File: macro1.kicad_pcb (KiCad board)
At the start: 2 copper layers, 65.9 x 38.1 mm, 24 parts, among them SW1 SW_Push, U1 ATmega32U4-A, Y1 Crystal

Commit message: First Route: NoKeys
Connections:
- U1 pad 27: unconnected-(U1-Pad27) -> ROW0
- U1 pad 28: unconnected-(U1-Pad28) -> COL1
- U1 pad 29: unconnected-(U1-Pad29) -> COL0
- U1 pad 30: unconnected-(U1-Pad30) -> ROW1
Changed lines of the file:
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@@
   (net 31 "unconnected-(U1-Pad25)")
   (net 32 "unconnected-(U1-Pad26)")
-  (net 33 "unconnected-(U1-Pad27)")
-  (net 34 "unconnected-(U1-Pad28)")
-  (net 35 "unconnected-(U1-Pad29)")
-  (net 36 "unconnected-(U1-Pad30)")
-  (net 37 "unconnected-(U1-Pad31)")
-  (net 38 "unconnected-(U1-Pad32)")
-  (net 39 "unconnected-(U1-Pad36)")
-  (net 40 "unconnected-(U1-Pad37)")
-  (net 41 "unconnected-(U1-Pad38)")
-  (net 42 "unconnected-(U1-Pad39)")
-  (net 43 "unconnected-(U1-Pad40)")
-  (net 44 "unconnected-(U1-Pad41)")
-  (net 45 "unconnected-(U1-Pad42)")
-  (net 46 "unconnected-(USB1-Pad2)")
-  (net 47 "Net-(U1-Pad4)")
+  (net 33 "unconnected-(U1-Pad31)")
+  (net 34 "unconnected-(U1-Pad32)")
+  (net 35 "unconnected-(U1-Pad36)")
+  (net 36 "unconnected-(U1-Pad37)")
+  (net 37 "unconnected-(U1-Pad38)")
+  (net 38 "unconnected-(U1-Pad39)")
+  (net 39 "unconnected-(U1-Pad40)")
+  (net 40 "unconnected-(U1-Pad41)")
+  (net 41 "unconnected-(U1-Pad42)")
+  (net 42 "unconnected-(USB1-Pad2)")
+  (net 43 "Net-(U1-Pad4)")
   (footprint "MX_Alps_Hybrid:MX-1U" (layer "F.Cu")
     (at 144.4625 101.6)
@@
       (net 17 "Net-(R3-Pad1)") (pinfunction "D-") (pintype "bidirectional"))
     (pad "4" smd rect (at -5.7 1.6 270) (size 1.5 0.55) (layers "B.Cu" "B.Paste" "B.Mask")
-      (net 47 "Net-(U1-Pad4)") (pinfunction "D+") (pintype "bidirectional"))
+      (net 43 "Net-(U1-Pad4)") (pinfunction "D+") (pintype "bidirectional"))
     (pad "5" smd rect (at -5.7 0.8 270) (size 1.5 0.55) (layers "B.Cu" "B.Paste" "B.Mask")
       (net 2 "GND") (pinfunction "UGND") (pintype "passive"))
@@
       (net 32 "unconnected-(U1-Pad26)") (pinfunction "PD6") (pintype "bidirectional+no_connect"))
     (pad "27" smd rect (at 5.7 -0.8 270) (size 1.5 0.55) (layers "B.Cu" "B.Paste" "B.Mask")
-      (net 33 "unconnected-(U1-Pad27)") (pinfunction "PD7") (pintype "bidirectional+no_connect"))
+      (net 6 "ROW0") (pinfunction "PD7") (pintype "bidirectional"))
     (pad "28" smd rect (at 5.7 0 270) (size 1.5 0.55) (layers "B.Cu" "B.Paste" "B.Mask")
-      (net 34 "unconnected-(U1-Pad28)") (pinfunction "PB4") (pintype "bidirectional+no_connect"))
+      (net 14 "COL1") (pinfunction "PB4") (pintype "bidirectional"))
     (pad "29" smd rect (at 5.7 0.8 270) (size 1.5 0.55) (layers "B.Cu" "B.Paste" "B.Mask")
-      (net 35 "unconnected-(U1-Pad29)") (pinfunction "PB5") (pintype "bidirectional+no_connect"))
+      (net 13 "COL0") (pinfunction "PB5") (pintype "bidirectional"))
     (pad "30" smd rect (at 5.7 1.6 270) (size 1.5 0.55) (layers "B.Cu" "B.Paste" "B.Mask")
-      (net 36 "unconnected-(U1-Pad30)") (pinfunction "PB6") (pintype "bidirectional+no_connect"))
+      (net 9 "ROW1") (pinfunction "PB6") (pintype "bidirectional"))
     (pad "31" smd rect (at 5.7 2.4 270) (size 1.5 0.55) (layers "B.Cu" "B.Paste" "B.Mask")
-      (net 37 "unconnected-(U1-Pad31)") (pinfunction "PC6") (pintype "bidirectional+no_connect"))
+      (net 33 "unconnected-(U1-Pad31)") (pinfunction "PC6") (pintype "bidirectional+no_connect"))
     (pad "32" smd rect (at 5.7 3.2 270) (size 1.5 0.55) (layers "B.Cu" "B.Paste" "B.Mask")
-      (net 38 "unconnected-(U1-Pad32)") (pinfunction "PC7") (pintype "bidirectional+no_connect"))
+      (net 34 "unconnected-(U1-Pad32)") (pinfunction "PC7") (pintype "bidirectional+no_connect"))
     (pad "33" smd rect (at 5.7 4 270) (size 1.5 0.55) (layers "B.Cu" "B.Paste" "B.Mask")
       (net 15 "Net-(R1-Pad1)") (pinfunction "~{HWB}/PE2") (pintype "bidirectional"))
@@
       (net 2 "GND") (pinfunction "GND") (pintype "passive"))
     (pad "36" smd rect (at 2.4 5.7 180) (size 1.5 0.55) (layers "B.Cu" "B.Paste" "B.Mask")
-      (net 39 "unconnected-(U1-Pad36)") (pinfunction "PF7") (pintype "bidirectional+no_connect"))
+      (net 35 "unconnected-(U1-Pad36)") (pinfunction "PF7") (pintype "bidirectional+no_connect"))
     (pad "37" smd rect (at 1.6 5.7 180) (size 1.5 0.55) (layers "B.Cu" "B.Paste" "B.Mask")
-      (net 40 "unconnected-(U1-Pad37)") (pinfunction "PF6") (pintype "bidirectional+no_connect"))
+      (net 36 "unconnected-(U1-Pad37)") (pinfunction "PF6") (pintype "bidirectional+no_connect"))
     (pad "38" smd rect (at 0.8 5.7 180) (size 1.5 0.55) (layers "B.Cu" "B.Paste" "B.Mask")
-      (net 41 "unconnected-(U1-Pad38)") (pinfunction "PF5") (pintype "bidirectional+no_connect"))
+      (net 37 "unconnected-(U1-Pad38)") (pinfunction "PF5") (pintype "bidirectional+no_connect"))
     (pad "39" smd rect (at 0 5.7 180) (size 1.5 0.55) (layers "B.Cu" "B.Paste" "B.Mask")
-      (net 42 "unconnected-(U1-Pad39)") (pinfunction "PF4") (pintype "bidirectional+no_connect"))
+      (net 38 "unconnected-(U1-Pad39)") (pinfunction "PF4") (pintype "bidirectional+no_connect"))
     (pad "40" smd rect (at -0.8 5.7 180) (size 1.5 0.55) (layers "B.Cu" "B.Paste" "B.Mask")
-      (net 43 "unconnected-(U1-Pad40)") (pinfunction "PF1") (pintype "bidirectional+no_connect"))
+      (net 39 "unconnected-(U1-Pad40)") (pinfunction "PF1") (pintype "bidirectional+no_connect"))
     (pad "41" smd rect (at -1.6 5.7 180) (size 1.5 0.55) (layers "B.Cu" "B.Paste" "B.Mask")
-      (net 44 "unconnected-(U1-Pad41)") (pinfunction "PF0") (pintype "bidirectional+no_connect"))
+      (net 40 "unconnected-(U1-Pad41)") (pinfunction "PF0") (pintype "bidirectional+no_connect"))
     (pad "42" smd rect (at -2.4 5.7 180) (size 1.5 0.55) (layers "B.Cu" "B.Paste" "B.Mask")
-      (net 45 "unconnected-(U1-Pad42)") (pinfunction "AREF") (pintype "passive+no_connect"))
+      (net 41 "unconnected-(U1-Pad42)") (pinfunction "AREF") (pintype "passive+no_connect"))
     (pad "43" smd rect (at -3.2 5.7 180) (size 1.5 0.55) (layers "B.Cu" "B.Paste" "B.Mask")
       (net 2 "GND") (pinfunction "GND") (pintype "passive"))
@@
       (net 2 "GND") (pinfunction "GND") (pintype "input"))
     (pad "2" smd rect locked (at 4.5 -0.8 270) (size 2.25 0.5) (layers "B.Cu" "B.Paste" "B.Mask")
-      (net 46 "unconnected-(USB1-Pad2)") (pinfunction "ID") (pintype "input+no_connect"))
+      (net 42 "unconnected-(USB1-Pad2)") (pinfunction "ID") (pintype "input+no_connect"))
     (pad "3" smd rect locked (at 4.5 0 270) (size 2.25 0.5) (layers "B.Cu" "B.Paste" "B.Mask")
       (net 18 "D-") (pinfunction "D+") (pintype "input"))
@@
       (net 16 "D+") (pintype "passive"))
     (pad "2" smd roundrect (at 0.9125 0 270) (size 1.025 1.4) (layers "B.Cu" "B.Paste" "B.Mask") (roundrect_rratio 0.243902)
-      (net 47 "Net-(U1-Pad4)") (pintype "passive"))
+      (net 43 "Net-(U1-Pad4)") (pintype "passive"))
     (model "${KICAD6_3DMODEL_DIR}/Resistor_SMD.3dshapes/R_0805_2012Metric.wrl"
       (offset (xyz 0 0 0))
@@
   (segment (start 109.4625 94.19375) (end 111.03825 94.19375) (width 0.254) (layer "B.Cu") (net 19))
   (segment (start 111.03825 94.19375) (end 111.125 94.107) (width 0.254) (layer "B.Cu") (net 19))
-  (segment (start 97.214239 104.834239) (end 97.214239 108.641333) (width 0.254) (layer "F.Cu") (net 47))
-  (segment (start 96.901 104.521) (end 97.214239 104.834239) (width 0.254) (layer "F.Cu") (net 47))
-  (via (at 96.901 104.521) (size 0.8) (drill 0.4) (layers "F.Cu" "B.Cu") (net 47))
-  (via (at 97.214239 108.641333) (size 0.8) (drill 0.4) (layers "F.Cu" "B.Cu") (net 47))
-  (segment (start 97.214239 108.641333) (end 97.89267 109.319764) (width 0.254) (layer "B.Cu") (net 47))
-  (segment (start 96.8375 103.30625) (end 96.8375 104.4575) (width 0.254) (layer "B.Cu") (net 47))
-  (segment (start 96.8375 104.4575) (end 96.901 104.521) (width 0.254) (layer "B.Cu") (net 47))
-  (segment (start 97.89267 109.319764) (end 97.89267 110.971289) (width 0.254) (layer "B.Cu") (net 47))
+  (segment (start 97.214239 104.834239) (end 97.214239 108.641333) (width 0.254) (layer "F.Cu") (net 43))
+  (segment (start 96.901 104.521) (end 97.214239 104.834239) (width 0.254) (layer "F.Cu") (net 43))
+  (via (at 96.901 104.521) (size 0.8) (drill 0.4) (layers "F.Cu" "B.Cu") (net 43))
+  (via (at 97.214239 108.641333) (size 0.8) (drill 0.4) (layers "F.Cu" "B.Cu") (net 43))
+  (segment (start 97.214239 108.641333) (end 97.89267 109.319764) (width 0.254) (layer "B.Cu") (net 43))
+  (segment (start 96.8375 103.30625) (end 96.8375 104.4575) (width 0.254) (layer "B.Cu") (net 43))
+  (segment (start 96.8375 104.4575) (end 96.901 104.521) (width 0.254) (layer "B.Cu") (net 43))
+  (segment (start 97.89267 109.319764) (end 97.89267 110.971289) (width 0.254) (layer "B.Cu") (net 43))
 )

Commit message: First Routing: Keys
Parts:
- turned D1 to 90 degrees
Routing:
- net COL1: track 0.00 -> 73.2 mm, vias 0 -> 2
- net ROW1: track 0.00 -> 54.8 mm, vias 0 -> 2
- net COL0: track 0.00 -> 53.5 mm, vias 0 -> 2
- net ROW0: track 0.00 -> 53.2 mm, vias 0 -> 2
- net Net-(MX4-Pad2): track 0.00 -> 11.9 mm
- net Net-(MX2-Pad2): track 0.00 -> 11.7 mm
- net Net-(D3-Pad2): track 0.00 -> 6.89 mm
- net Net-(MX1-Pad2): track 0.00 -> 6.61 mm
- net +5V: track 108.8 -> 106.8 mm, vias 10 -> 8

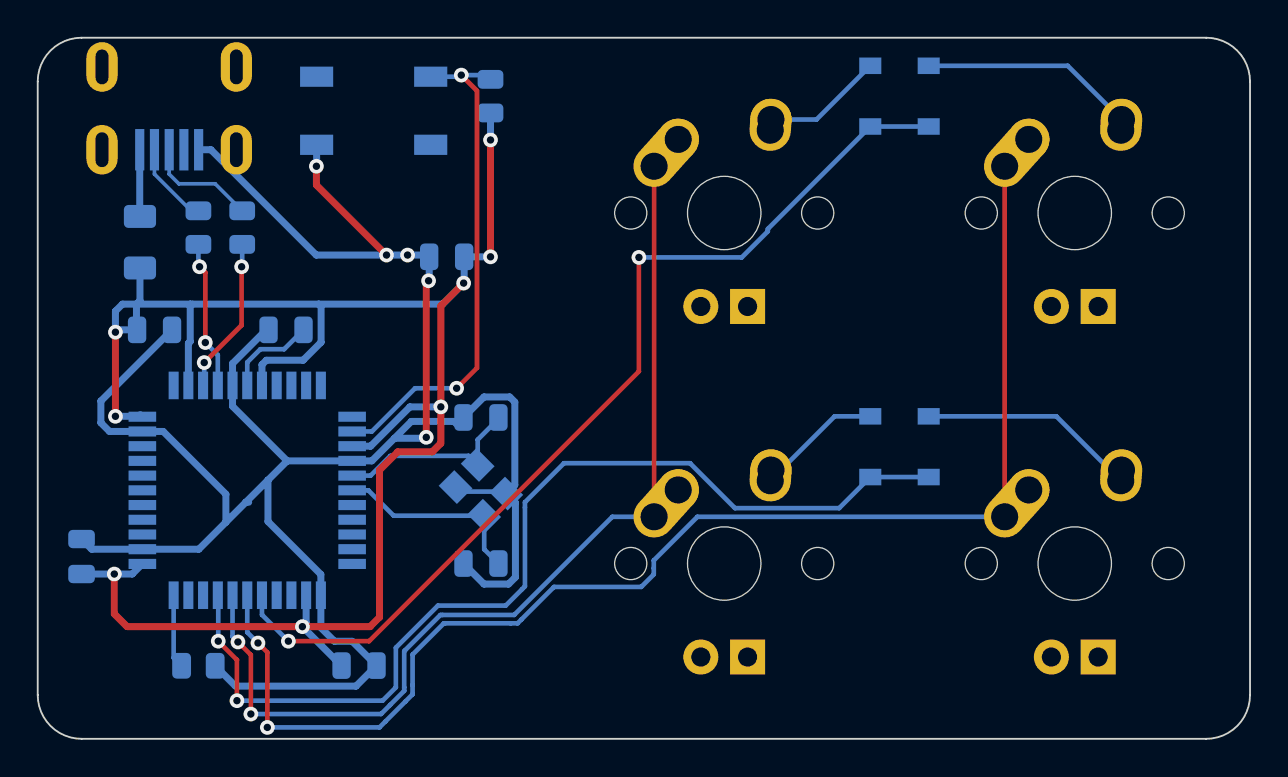
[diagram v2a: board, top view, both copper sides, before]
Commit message: First Routing: Keys
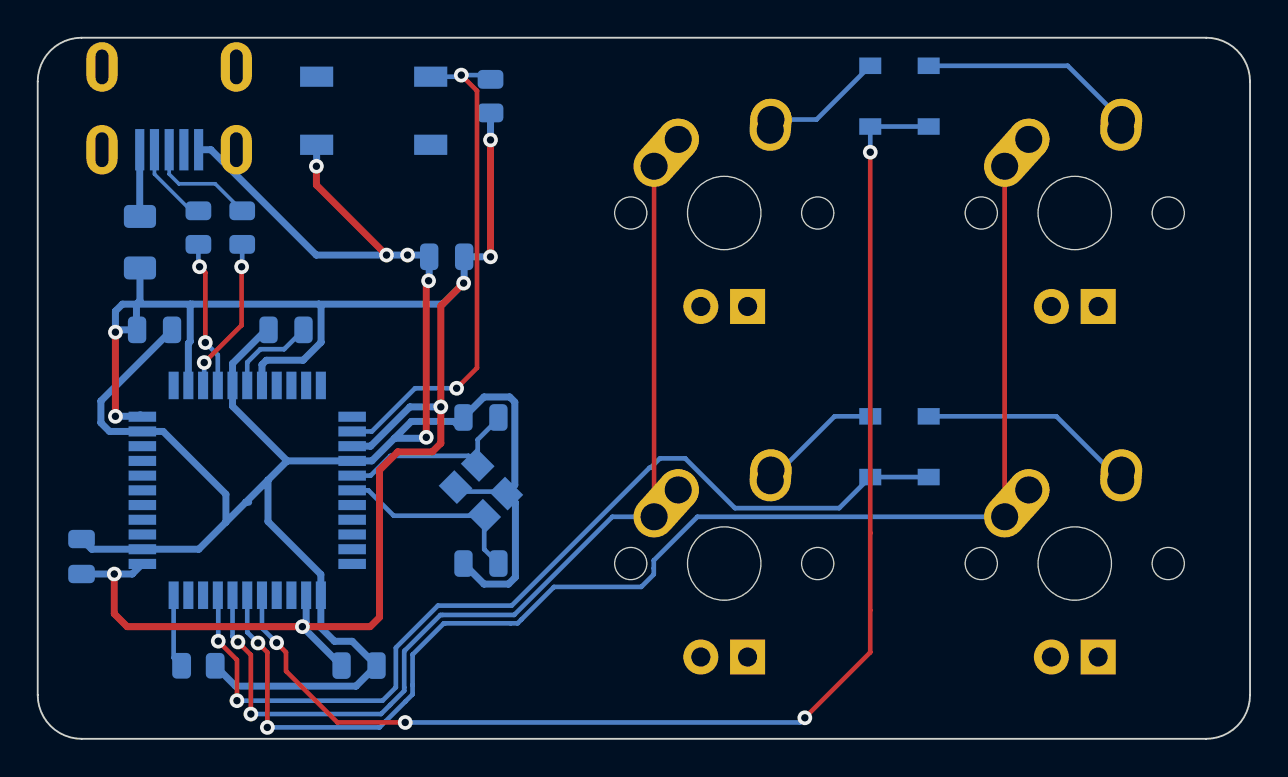
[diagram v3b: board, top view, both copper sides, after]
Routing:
- net ROW0: track 53.2 -> 70.9 mm, vias 2 -> 4
- net ROW1: track 54.8 -> 52.3 mm
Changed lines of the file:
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@@
   (segment (start 112.015893 113.917107) (end 112.015893 115.292431) (width 0.254) (layer "B.Cu") (net 5))
   (segment (start 106.19667 115.871289) (end 105.19267 115.871289) (width 0.254) (layer "B.Cu") (net 5))
-  (segment (start 120.777 110.205856) (end 106.113856 124.869) (width 0.254) (layer "F.Cu") (net 6))
-  (segment (start 106.113856 124.869) (end 101.727 124.869) (width 0.254) (layer "F.Cu") (net 6))
-  (segment (start 120.777 104.013) (end 120.777 110.205856) (width 0.254) (layer "F.Cu") (net 6))
-  (via (at 101.727 124.869) (size 0.8) (drill 0.4) (layers "F.Cu" "B.Cu") (net 6))
-  (via (at 120.777 104.013) (size 0.8) (drill 0.4) (layers "F.Cu" "B.Cu") (net 6))
-  (segment (start 127.783401 102.594599) (end 126.365 104.013) (width 0.254) (layer "B.Cu") (net 6))
-  (segment (start 100.29267 123.43467) (end 100.29267 122.371289) (width 0.254) (layer "B.Cu") (net 6))
-  (segment (start 101.727 124.869) (end 100.29267 123.43467) (width 0.254) (layer "B.Cu") (net 6))
+  (segment (start 133.35 118.999) (end 133.35 123.19) (width 0.254) (layer "F.Cu") (net 6))
+  (segment (start 101.6 126.492) (end 101.6 125.476) (width 0.254) (layer "F.Cu") (net 6))
+  (segment (start 101.089465 124.965465) (end 101.089465 124.954038) (width 0.254) (layer "F.Cu") (net 6))
+  (segment (start 133.35 123.19) (end 133.35 125.476) (width 0.254) (layer "F.Cu") (net 6))
+  (segment (start 133.35 125.476) (end 129.794 129.032) (width 0.254) (layer "F.Cu") (net 6))
+  (segment (start 133.35 98.298) (end 133.35 118.999) (width 0.254) (layer "F.Cu") (net 6))
+  (segment (start 104.394 129.286) (end 101.6 126.492) (width 0.254) (layer "F.Cu") (net 6))
+  (segment (start 101.6 125.476) (end 101.089465 124.965465) (width 0.254) (layer "F.Cu") (net 6))
+  (segment (start 108.077 129.286) (end 104.394 129.286) (width 0.254) (layer "F.Cu") (net 6))
+  (via (at 129.794 129.032) (size 0.8) (drill 0.4) (layers "F.Cu" "B.Cu") (net 6))
+  (via (at 133.35 98.298) (size 0.8) (drill 0.4) (layers "F.Cu" "B.Cu") (net 6))
+  (via (at 101.089465 124.954038) (size 0.8) (drill 0.4) (layers "F.Cu" "B.Cu") (net 6))
+  (via (at 108.077 129.286) (size 0.8) (drill 0.4) (layers "F.Cu" "B.Cu") (net 6))
+  (segment (start 101.089465 124.954038) (end 100.29267 124.157243) (width 0.254) (layer "B.Cu") (net 6))
   (segment (start 133.35 96.9) (end 136.525 96.9) (width 0.254) (layer "B.Cu") (net 6))
-  (segment (start 133.35 96.9) (end 127.783401 102.466599) (width 0.254) (layer "B.Cu") (net 6))
-  (segment (start 126.365 104.013) (end 120.777 104.013) (width 0.254) (layer "B.Cu") (net 6))
-  (segment (start 127.783401 102.466599) (end 127.783401 102.594599) (width 0.254) (layer "B.Cu") (net 6))
+  (segment (start 100.29267 124.157243) (end 100.29267 122.371289) (width 0.254) (layer "B.Cu") (net 6))
+  (segment (start 129.54 129.286) (end 108.077 129.286) (width 0.254) (layer "B.Cu") (net 6))
+  (segment (start 133.35 96.9) (end 133.35 98.298) (width 0.254) (layer "B.Cu") (net 6))
+  (segment (start 129.794 129.032) (end 129.54 129.286) (width 0.254) (layer "B.Cu") (net 6))
   (segment (start 130.43 96.52) (end 133.35 93.6) (width 0.254) (layer "B.Cu") (net 7))
   (segment (start 127.9525 96.52) (end 130.43 96.52) (width 0.254) (layer "B.Cu") (net 7))
@@
   (via (at 97.917 124.869) (size 0.8) (drill 0.4) (layers "F.Cu" "B.Cu") (net 9))
   (via (at 98.933 128.101789) (size 0.8) (drill 0.4) (layers "F.Cu" "B.Cu") (net 9))
-  (segment (start 114.427 122.047) (end 113.538 122.936) (width 0.254) (layer "B.Cu") (net 9))
+  (segment (start 125.998866 117.639939) (end 131.660061 117.639939) (width 0.254) (layer "B.Cu") (net 9))
+  (segment (start 121.356255 115.443) (end 121.412 115.443) (width 0.254) (layer "B.Cu") (net 9))
   (segment (start 136.525 115.95) (end 133.35 115.95) (width 0.254) (layer "B.Cu") (net 9))
-  (segment (start 114.584004 121.889996) (end 114.427 122.047) (width 0.254) (layer "B.Cu") (net 9))
-  (segment (start 123.556927 115.198) (end 116.704 115.198) (width 0.254) (layer "B.Cu") (net 9))
-  (segment (start 125.998866 117.639939) (end 123.556927 115.198) (width 0.254) (layer "B.Cu") (net 9))
-  (segment (start 106.848211 128.101789) (end 98.933 128.101789) (width 0.254) (layer "B.Cu") (net 9))
-  (segment (start 133.35 115.95) (end 131.660061 117.639939) (width 0.254) (layer "B.Cu") (net 9))
-  (segment (start 107.569 127.381) (end 106.848211 128.101789) (width 0.254) (layer "B.Cu") (net 9))
-  (segment (start 131.660061 117.639939) (end 125.998866 117.639939) (width 0.254) (layer "B.Cu") (net 9))
+  (segment (start 121.412 115.443) (end 121.92 114.935) (width 0.254) (layer "B.Cu") (net 9))
   (segment (start 97.917 122.395619) (end 97.89267 122.371289) (width 0.254) (layer "B.Cu") (net 9))
-  (segment (start 109.855 122.936) (end 107.569 125.222) (width 0.254) (layer "B.Cu") (net 9))
-  (segment (start 114.584004 117.317996) (end 114.584004 117.602) (width 0.254) (layer "B.Cu") (net 9))
-  (segment (start 116.704 115.198) (end 114.584004 117.317996) (width 0.254) (layer "B.Cu") (net 9))
-  (segment (start 113.538 122.936) (end 109.855 122.936) (width 0.254) (layer "B.Cu") (net 9))
-  (segment (start 107.569 125.222) (end 107.569 127.381) (width 0.254) (layer "B.Cu") (net 9))
-  (segment (start 114.584004 117.602) (end 114.584004 121.889996) (width 0.254) (layer "B.Cu") (net 9))
+  (segment (start 121.92 114.935) (end 123.293927 114.935) (width 0.254) (layer "B.Cu") (net 9))
+  (segment (start 107.569 127.381) (end 107.569 125.222) (width 0.254) (layer "B.Cu") (net 9))
+  (segment (start 123.293927 114.935) (end 125.998866 117.639939) (width 0.254) (layer "B.Cu") (net 9))
+  (segment (start 106.848211 128.101789) (end 107.569 127.381) (width 0.254) (layer "B.Cu") (net 9))
+  (segment (start 109.855 122.936) (end 113.863255 122.936) (width 0.254) (layer "B.Cu") (net 9))
+  (segment (start 131.660061 117.639939) (end 133.35 115.95) (width 0.254) (layer "B.Cu") (net 9))
+  (segment (start 107.569 125.222) (end 109.855 122.936) (width 0.254) (layer "B.Cu") (net 9))
+  (segment (start 113.863255 122.936) (end 121.356255 115.443) (width 0.254) (layer "B.Cu") (net 9))
+  (segment (start 98.933 128.101789) (end 106.848211 128.101789) (width 0.254) (layer "B.Cu") (net 9))
   (segment (start 97.917 124.869) (end 97.917 122.395619) (width 0.254) (layer "B.Cu") (net 9))
   (segment (start 127.9125 116.15) (end 131.4125 112.65) (width 0.254) (layer "B.Cu") (net 10))

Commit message: Finished Product 1
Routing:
- net +5V: track 106.8 -> 104.7 mm
- net GND: track 126.2 -> 124.8 mm, vias 5 -> 4
- added copper zone on B.Cu, net GND
